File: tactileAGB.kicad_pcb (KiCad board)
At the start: 2 copper layers, 33.2 x 49 mm, 21 parts

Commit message: Fixed naming of testpoint VDD-15
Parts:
- renumbered VDD15 to VDD-15
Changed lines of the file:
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@@
       (effects (font (size 1 1) (thickness 0.15)))
     )
-    (fp_line (start -2.5 -1.65) (end -2.5 1.65) (layer F.SilkS) (width 0.12))
-    (fp_line (start -2.3 2.5) (end 2.3 2.5) (layer F.SilkS) (width 0.12))
-    (fp_line (start 2.5 1.65) (end 2.5 -1.65) (layer F.SilkS) (width 0.12))
-    (fp_line (start 2.3 -2.5) (end -2.3 -2.5) (layer F.SilkS) (width 0.12))
+    (fp_line (start 2.3 -2.5) (end -2.3 -2.5) (layer F.SilkS) (width 0.12))
+    (fp_line (start 2.5 1.65) (end 2.5 -1.65) (layer F.SilkS) (width 0.12))
+    (fp_line (start -2.3 2.5) (end 2.3 2.5) (layer F.SilkS) (width 0.12))
+    (fp_line (start -2.5 -1.65) (end -2.5 1.65) (layer F.SilkS) (width 0.12))
     (pad 4 smd rect (at -3.5 -2.2 270) (size 2 0.7) (layers F.Cu F.Paste F.Mask)
       (net 1 GND3))
@@
       (effects (font (size 1 1) (thickness 0.15)))
     )
-    (fp_line (start -2.5 -1.65) (end -2.5 1.65) (layer F.SilkS) (width 0.12))
-    (fp_line (start -2.3 2.5) (end 2.3 2.5) (layer F.SilkS) (width 0.12))
-    (fp_line (start 2.5 1.65) (end 2.5 -1.65) (layer F.SilkS) (width 0.12))
-    (fp_line (start 2.3 -2.5) (end -2.3 -2.5) (layer F.SilkS) (width 0.12))
+    (fp_line (start 2.3 -2.5) (end -2.3 -2.5) (layer F.SilkS) (width 0.12))
+    (fp_line (start 2.5 1.65) (end 2.5 -1.65) (layer F.SilkS) (width 0.12))
+    (fp_line (start -2.3 2.5) (end 2.3 2.5) (layer F.SilkS) (width 0.12))
+    (fp_line (start -2.5 -1.65) (end -2.5 1.65) (layer F.SilkS) (width 0.12))
     (pad 4 smd rect (at -3.5 -2.2 90) (size 2 0.7) (layers F.Cu F.Paste F.Mask)
       (net 1 GND3))
@@
       (effects (font (size 1 1) (thickness 0.15)))
     )
-    (fp_line (start -2.5 -1.65) (end -2.5 1.65) (layer F.SilkS) (width 0.12))
-    (fp_line (start -2.3 2.5) (end 2.3 2.5) (layer F.SilkS) (width 0.12))
-    (fp_line (start 2.5 1.65) (end 2.5 -1.65) (layer F.SilkS) (width 0.12))
-    (fp_line (start 2.3 -2.5) (end -2.3 -2.5) (layer F.SilkS) (width 0.12))
+    (fp_line (start 2.3 -2.5) (end -2.3 -2.5) (layer F.SilkS) (width 0.12))
+    (fp_line (start 2.5 1.65) (end 2.5 -1.65) (layer F.SilkS) (width 0.12))
+    (fp_line (start -2.3 2.5) (end 2.3 2.5) (layer F.SilkS) (width 0.12))
+    (fp_line (start -2.5 -1.65) (end -2.5 1.65) (layer F.SilkS) (width 0.12))
     (pad 4 smd rect (at -3.5 -2.2) (size 2 0.7) (layers F.Cu F.Paste F.Mask)
       (net 4 GND1))
@@
       (effects (font (size 1 1) (thickness 0.15)))
     )
-    (fp_line (start -2.5 -1.65) (end -2.5 1.65) (layer F.SilkS) (width 0.12))
-    (fp_line (start -2.3 2.5) (end 2.3 2.5) (layer F.SilkS) (width 0.12))
-    (fp_line (start 2.5 1.65) (end 2.5 -1.65) (layer F.SilkS) (width 0.12))
-    (fp_line (start 2.3 -2.5) (end -2.3 -2.5) (layer F.SilkS) (width 0.12))
+    (fp_line (start 2.3 -2.5) (end -2.3 -2.5) (layer F.SilkS) (width 0.12))
+    (fp_line (start 2.5 1.65) (end 2.5 -1.65) (layer F.SilkS) (width 0.12))
+    (fp_line (start -2.3 2.5) (end 2.3 2.5) (layer F.SilkS) (width 0.12))
+    (fp_line (start -2.5 -1.65) (end -2.5 1.65) (layer F.SilkS) (width 0.12))
     (pad 4 smd rect (at -3.5 -2.2 270) (size 2 0.7) (layers F.Cu F.Paste F.Mask)
       (net 4 GND1))
@@
       (effects (font (size 1 1) (thickness 0.15)))
     )
-    (fp_line (start -2.5 -1.65) (end -2.5 1.65) (layer F.SilkS) (width 0.12))
-    (fp_line (start -2.3 2.5) (end 2.3 2.5) (layer F.SilkS) (width 0.12))
-    (fp_line (start 2.5 1.65) (end 2.5 -1.65) (layer F.SilkS) (width 0.12))
-    (fp_line (start 2.3 -2.5) (end -2.3 -2.5) (layer F.SilkS) (width 0.12))
+    (fp_line (start 2.3 -2.5) (end -2.3 -2.5) (layer F.SilkS) (width 0.12))
+    (fp_line (start 2.5 1.65) (end 2.5 -1.65) (layer F.SilkS) (width 0.12))
+    (fp_line (start -2.3 2.5) (end 2.3 2.5) (layer F.SilkS) (width 0.12))
+    (fp_line (start -2.5 -1.65) (end -2.5 1.65) (layer F.SilkS) (width 0.12))
     (pad 4 smd rect (at -3.5 -2.2 90) (size 2 0.7) (layers F.Cu F.Paste F.Mask)
       (net 4 GND1))
@@
       (effects (font (size 1 1) (thickness 0.15)))
     )
+    (fp_line (start -1.95 -0.85) (end -1.95 0.85) (layer F.SilkS) (width 0.12))
+    (fp_line (start 1.95 1.9) (end -1.95 1.9) (layer F.SilkS) (width 0.12))
+    (fp_line (start 1.95 -0.85) (end 1.95 0.85) (layer F.SilkS) (width 0.12))
     (fp_line (start -1.95 -1.9) (end 1.95 -1.9) (layer F.SilkS) (width 0.12))
-    (fp_line (start 1.95 -0.85) (end 1.95 0.85) (layer F.SilkS) (width 0.12))
-    (fp_line (start 1.95 1.9) (end -1.95 1.9) (layer F.SilkS) (width 0.12))
-    (fp_line (start -1.95 -0.85) (end -1.95 0.85) (layer F.SilkS) (width 0.12))
     (pad 4 smd rect (at -2.25 -1.375) (size 2 0.65) (layers F.Cu F.Paste F.Mask)
       (net 8 GND2))
@@
       (effects (font (size 1 1) (thickness 0.15)))
     )
+    (fp_line (start -1.95 -0.85) (end -1.95 0.85) (layer F.SilkS) (width 0.12))
+    (fp_line (start 1.95 1.9) (end -1.95 1.9) (layer F.SilkS) (width 0.12))
+    (fp_line (start 1.95 -0.85) (end 1.95 0.85) (layer F.SilkS) (width 0.12))
     (fp_line (start -1.95 -1.9) (end 1.95 -1.9) (layer F.SilkS) (width 0.12))
-    (fp_line (start 1.95 -0.85) (end 1.95 0.85) (layer F.SilkS) (width 0.12))
-    (fp_line (start 1.95 1.9) (end -1.95 1.9) (layer F.SilkS) (width 0.12))
-    (fp_line (start -1.95 -0.85) (end -1.95 0.85) (layer F.SilkS) (width 0.12))
     (pad 4 smd rect (at -2.25 -1.375 180) (size 2 0.65) (layers F.Cu F.Paste F.Mask)
       (net 8 GND2))
@@
       (effects (font (size 1 1) (thickness 0.15)))
     )
-    (fp_line (start -2.5 -1.65) (end -2.5 1.65) (layer F.SilkS) (width 0.12))
-    (fp_line (start -2.3 2.5) (end 2.3 2.5) (layer F.SilkS) (width 0.12))
-    (fp_line (start 2.5 1.65) (end 2.5 -1.65) (layer F.SilkS) (width 0.12))
-    (fp_line (start 2.3 -2.5) (end -2.3 -2.5) (layer F.SilkS) (width 0.12))
+    (fp_line (start 2.3 -2.5) (end -2.3 -2.5) (layer F.SilkS) (width 0.12))
+    (fp_line (start 2.5 1.65) (end 2.5 -1.65) (layer F.SilkS) (width 0.12))
+    (fp_line (start -2.3 2.5) (end 2.3 2.5) (layer F.SilkS) (width 0.12))
+    (fp_line (start -2.5 -1.65) (end -2.5 1.65) (layer F.SilkS) (width 0.12))
     (pad 4 smd rect (at -3.5 -2.2 180) (size 2 0.7) (layers F.Cu F.Paste F.Mask)
       (net 4 GND1))
@@
   (module AGBTactile:Hole-1.5mm (layer F.Cu)
     (at 63.972506 63.385768)
-    (fp_text reference VDD15 (at -4.122506 1.344232) (layer F.SilkS) hide
-      (effects (font (size 1 1) (thickness 0.15)))
-    )
+    (fp_text reference VDD-15 (at -4.122506 1.344232) (layer F.SilkS) hide
+      (effects (font (size 1 1) (thickness 0.15)))
+    )

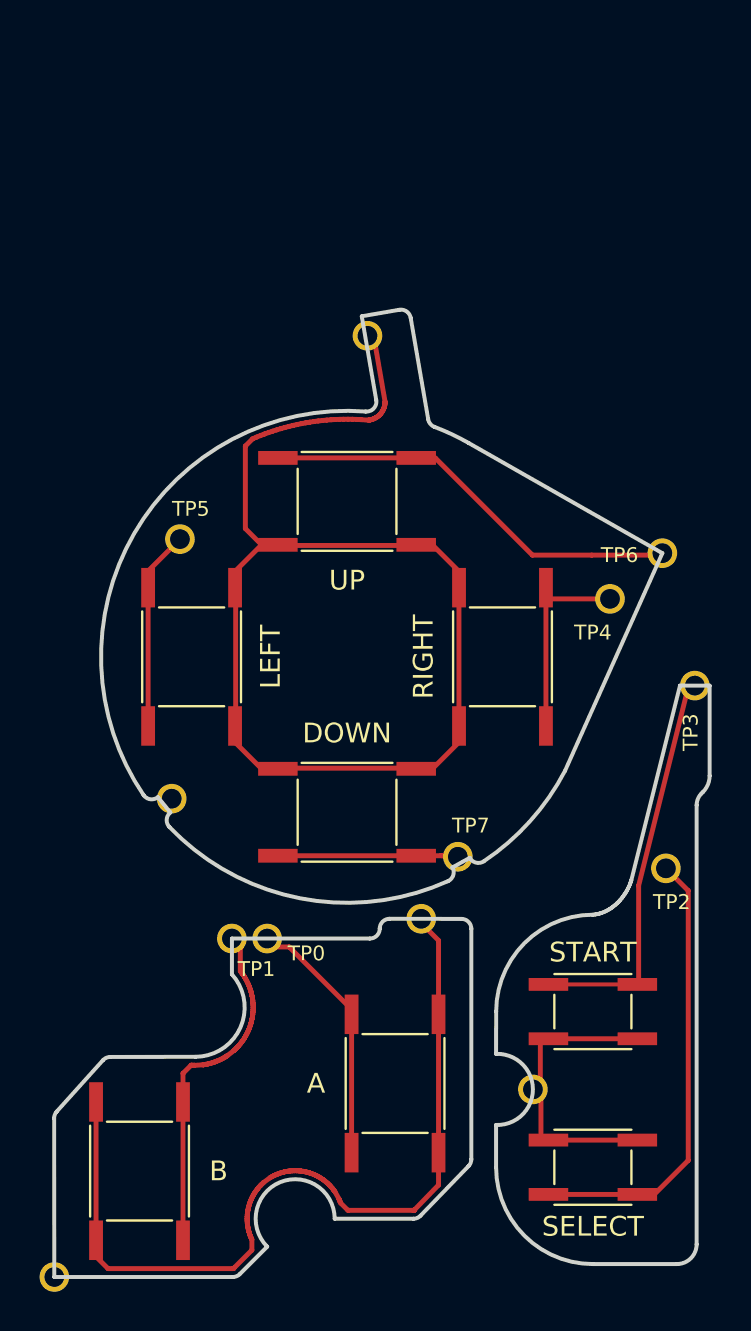
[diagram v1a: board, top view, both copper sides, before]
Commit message: Reduced gerber size to lower OSH Park cost
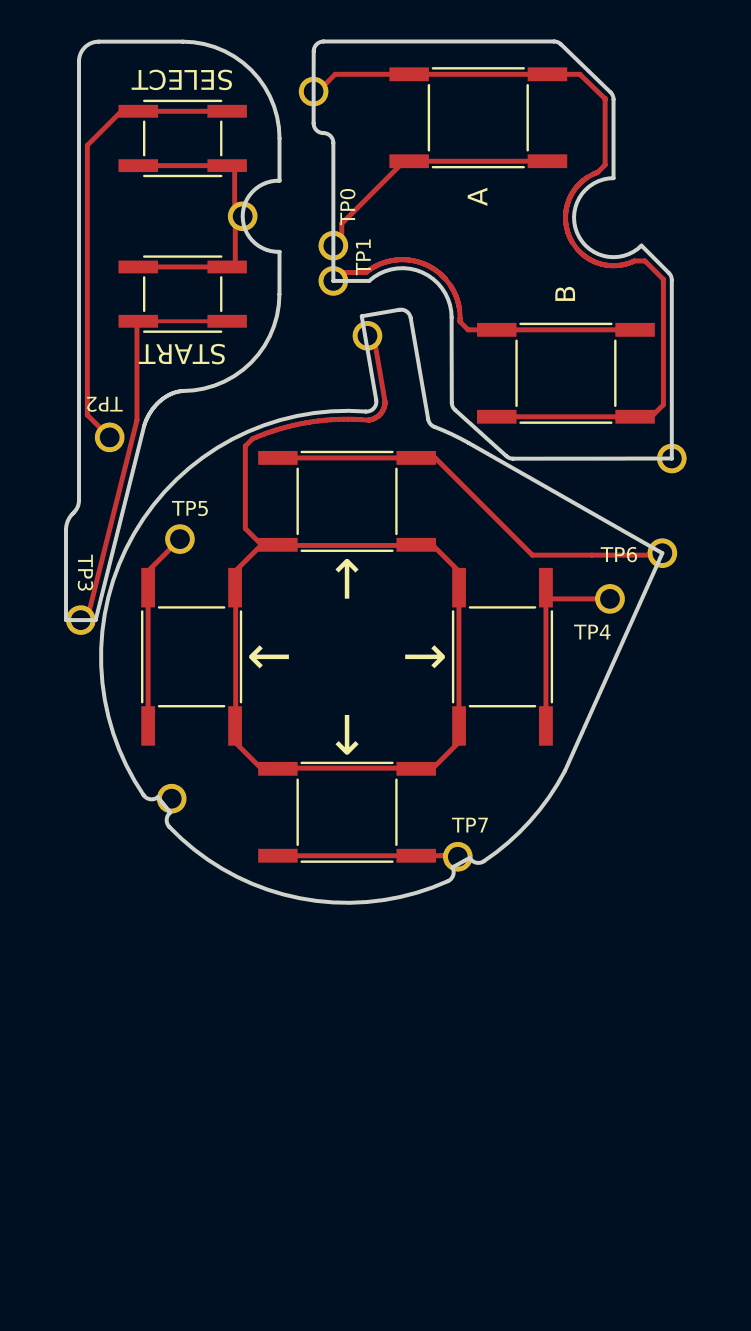
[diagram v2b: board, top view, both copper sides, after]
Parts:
- moved SELECT 56.1 mm to (64.5, 30.0), turned to 180 degrees
- moved FR2 51.9 mm to (89.3, 46.2), turned to 90 degrees
- moved A 49.1 mm to (79.5, 28.9), turned to 0 degrees
- moved GND2PAD1 46.6 mm to (67.6, 33.9), turned to 180 degrees
- moved B 45.8 mm to (83.9, 41.9), turned to 180 degrees
- moved GND3PAD1 42.2 mm to (71.2, 27.6), turned to 90 degrees
- moved START 41.8 mm to (64.5, 37.8), turned to 0 degrees
- moved TP2 35.6 mm to (60.8, 45.1), turned to 180 degrees
- moved TP0 35.2 mm to (72.2, 35.4), turned to 90 degrees
- moved TP1 33.7 mm to (72.2, 37.2), turned to 90 degrees
- moved TP3 31.3 mm to (59.4, 54.3), turned to 180 degrees
- renumbered DOWN to ↑, LEFT to ↑, RIGHT to ↑, UP to ↑
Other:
- board size 33.2 x 49 mm -> 30.7 x 43.6 mm

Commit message: Rev 1.1 - changed to GBA SP buttons, removed NoStartSelect gerber option
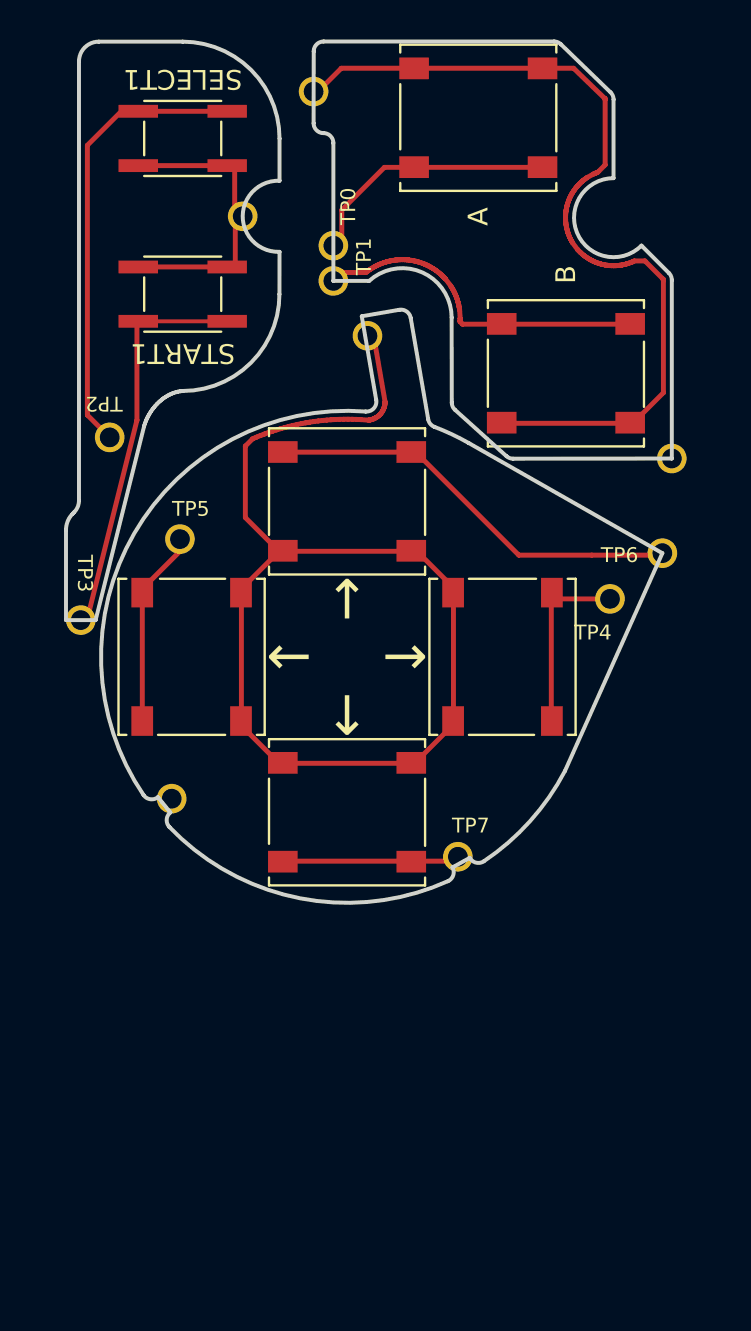
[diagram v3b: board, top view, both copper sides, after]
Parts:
- A, B, ↑ (x4): value PTS526 SM08 SMTR2 LFS -> SKRRABE010; footprint AGBTactile:PTS526 Sx08 SMTR2 LFS -> tactileAGB:SKRRABE010
- SELECT1: renamed from SELECT; footprint AGBTactile:SOG-15xANT -> tactileAGB:SOG-15xANT
- START1: renamed from START; footprint AGBTactile:SOG-15xANT -> tactileAGB:SOG-15xANT
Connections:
- FR2 pad 1: (no net) -> Net-(FR2-Pad1)
- VDD-15 pad 1: (no net) -> Net-(VDD-15-Pad1)
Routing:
- net GND1: track 58.9 -> 54.0 mm
- net Net-(LEFT1-Pad1): track 10.2 -> 8.58 mm
- net Net-(DOWN1-Pad1): track 9.19 -> 7.84 mm
- net Net-(TP6-Pad1): track 21.2 -> 20.4 mm
- net Net-(B1-Pad1): track 17.2 -> 16.5 mm
- net GND3: track 42.8 -> 42.2 mm
